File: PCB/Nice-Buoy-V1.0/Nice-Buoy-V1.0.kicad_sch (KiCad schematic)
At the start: 4 parts

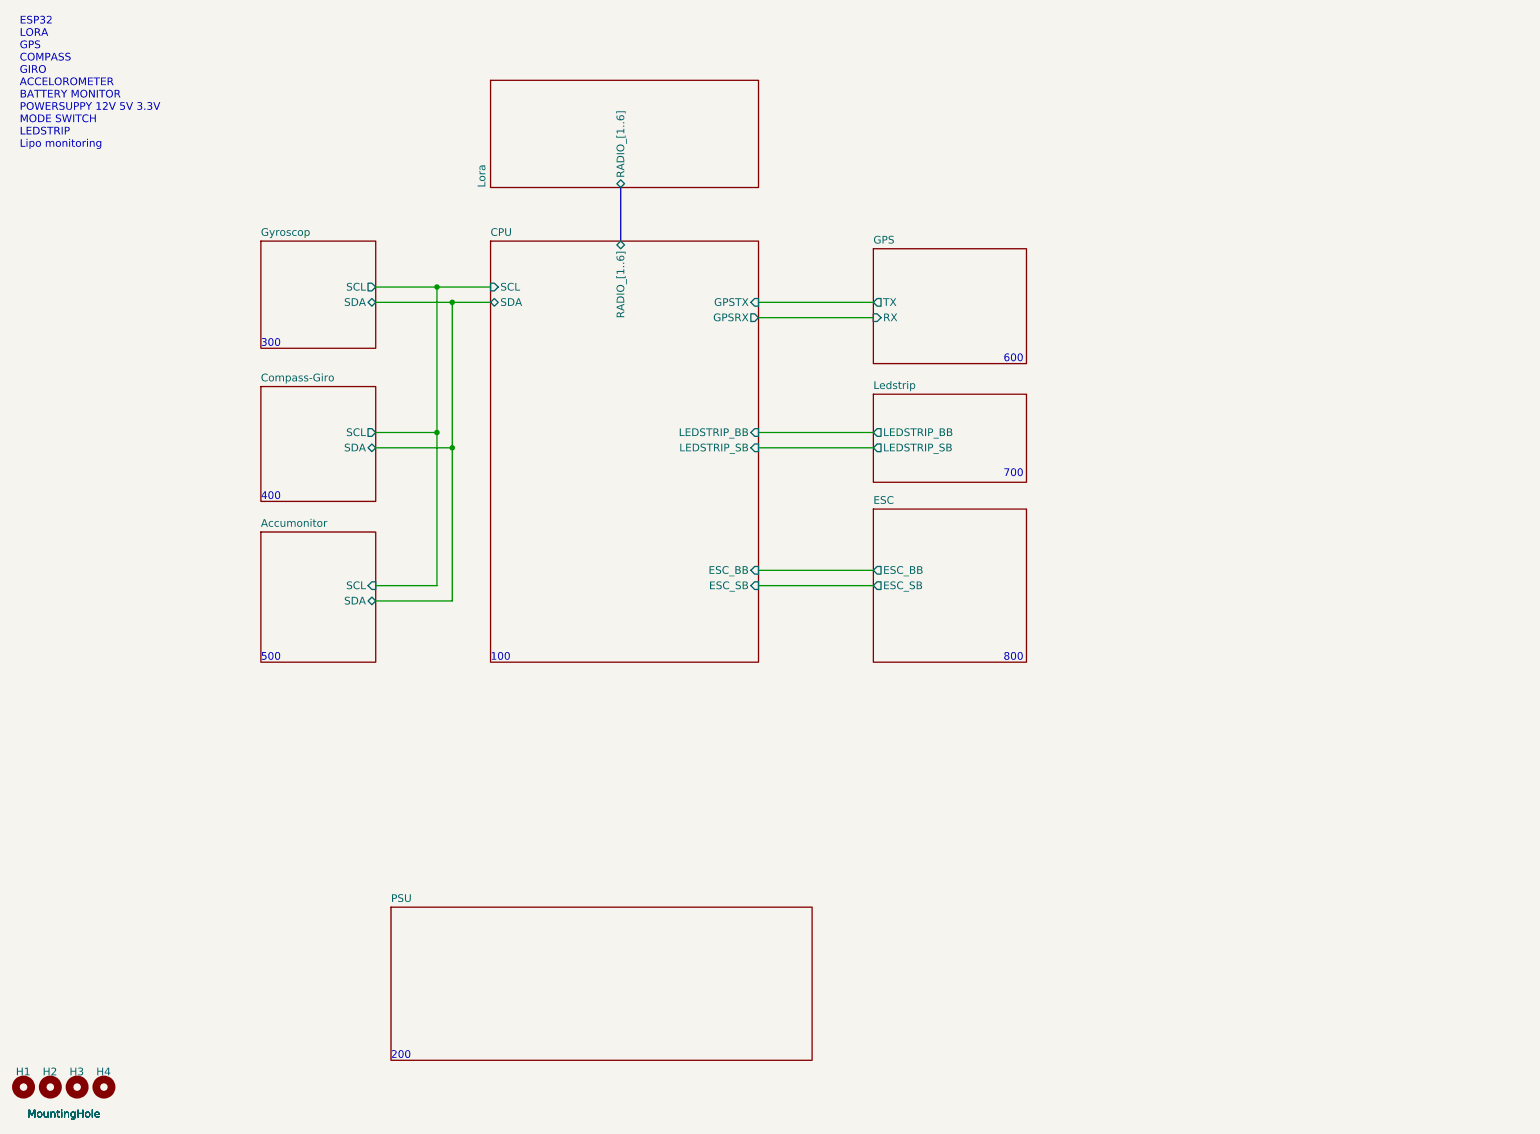
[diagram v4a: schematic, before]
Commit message: Battery monitor not working
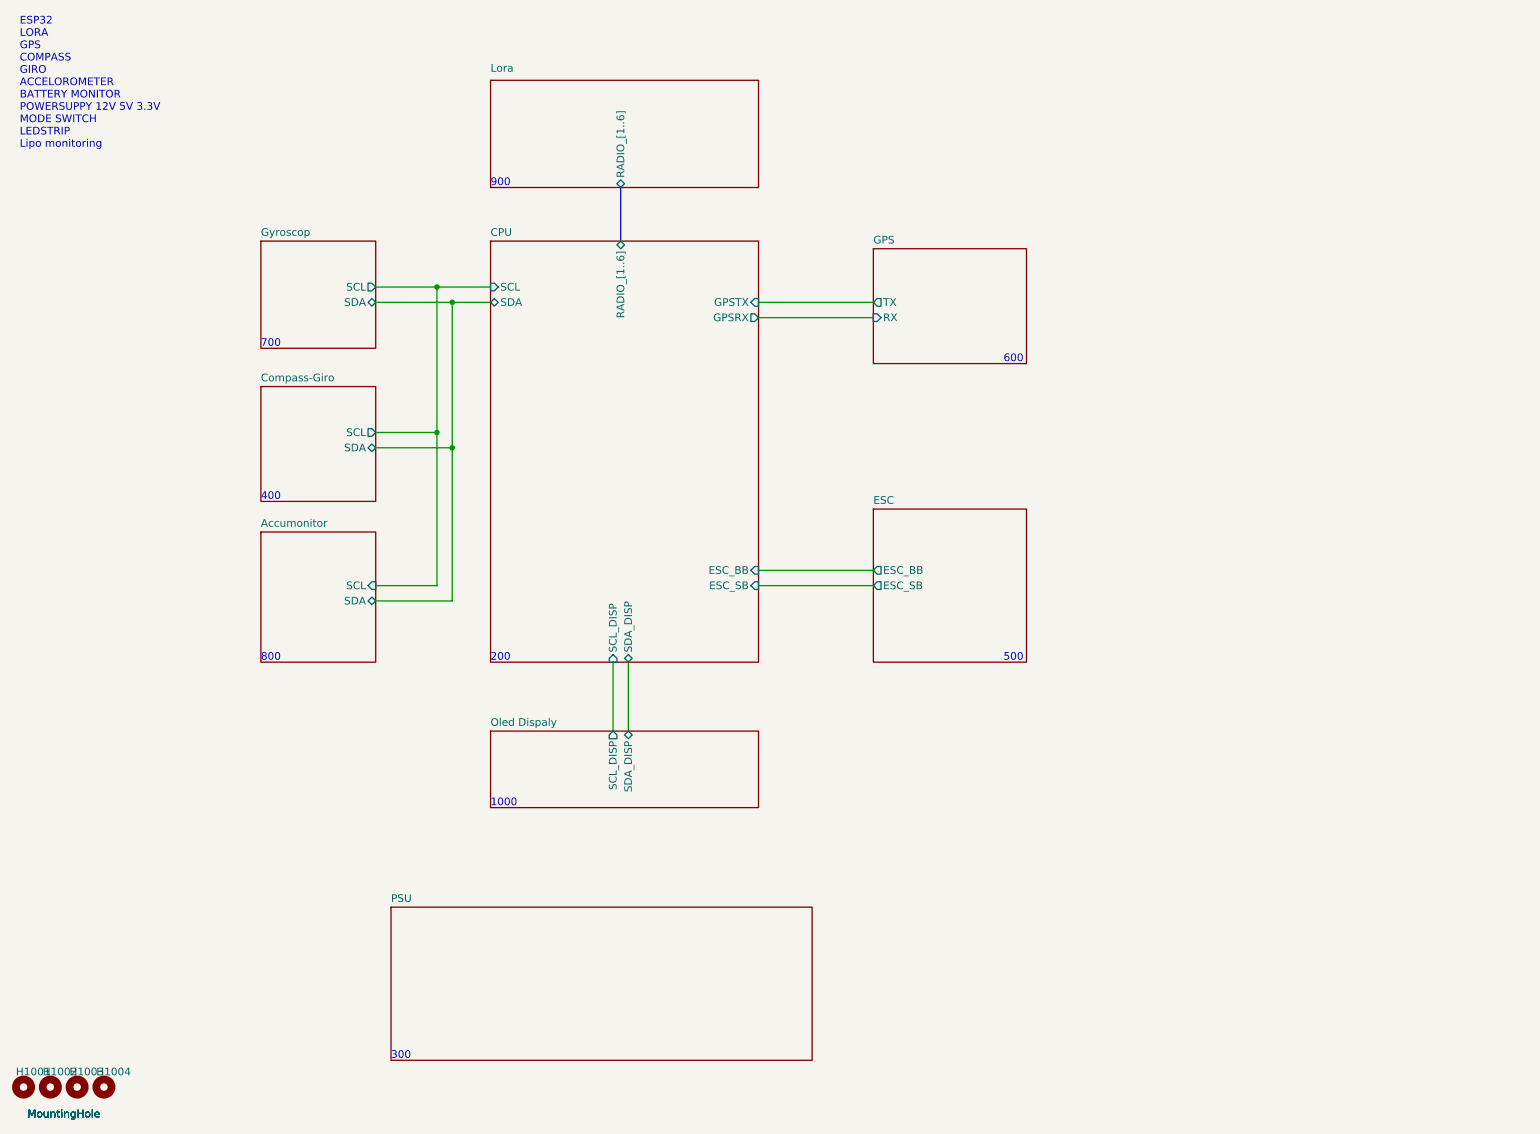
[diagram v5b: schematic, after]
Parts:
- renumbered H1 to H1001, H2 to H1002, H3 to H1003, H4 to H1004
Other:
- removed sheet Ledstrip
- added sheet Oled Dispaly (OledDispaly.kicad_sch)
- sheet Accumonitor: file untitled.kicad_sch -> Accumonitor.kicad_sch
- sheet CPU ports: added SCL_DISP, SDA_DISP; removed LEDSTRIP_BB, LEDSTRIP_SB
- note added: "1000"
- note added: "900"
- note removed: "100"

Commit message: Routing finnished
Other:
- sheet Accumonitor ports: added Vbatt; removed none
- sheet CPU ports: added Vbatt; removed none
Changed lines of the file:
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@@
+    (stroke (width 0) (type default))
+  )
+  (wire (pts (xy 76.2 113.03) (xy 95.25 113.03))
     (stroke (width 0) (type default))
   )
@@
       (effects (font (size 1.27 1.27)) (justify right))
     )
+    (pin "Vbatt" input (at 76.2 113.03 0)
+      (effects (font (size 1.27 1.27)) (justify right))
+    )
     (instances
       (project "Nice-Buoy-V1.0"
@@
       (effects (font (size 1.27 1.27)) (justify left))
     )
+    (pin "Vbatt" output (at 95.25 113.03 180)
+      (effects (font (size 1.27 1.27)) (justify left))
+    )
